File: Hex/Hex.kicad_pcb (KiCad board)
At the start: 2 copper layers, 114 x 88.2 mm, 39 parts, among them SW0x0 SW_Push, SW0x1 SW_Push, SW0x2 SW_Push, SW0x3 SW_Push, SW1x0 SW_Push, SW1x1 SW_Push, SW1x2 SW_Push, SW1x3 SW_Push, SW2x0 SW_Push, SW2x1 SW_Push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

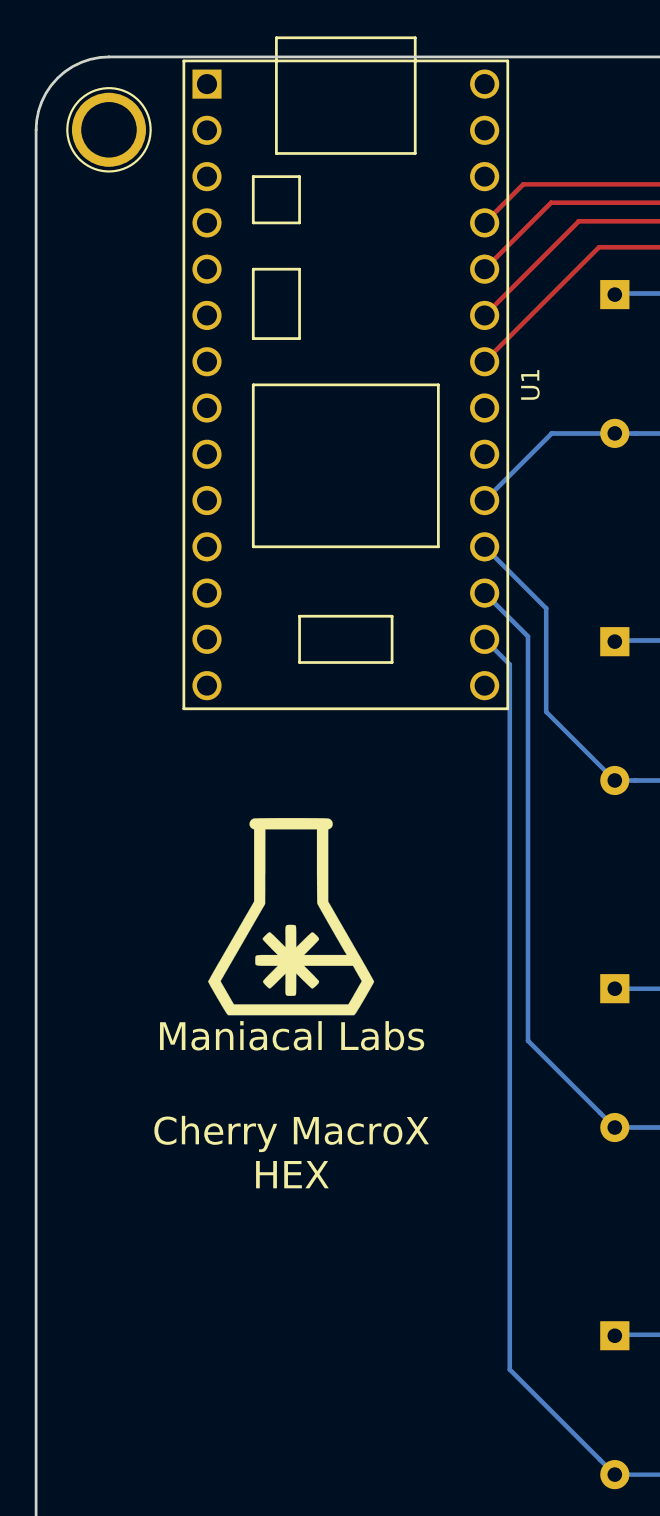
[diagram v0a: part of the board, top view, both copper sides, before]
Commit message: move logos
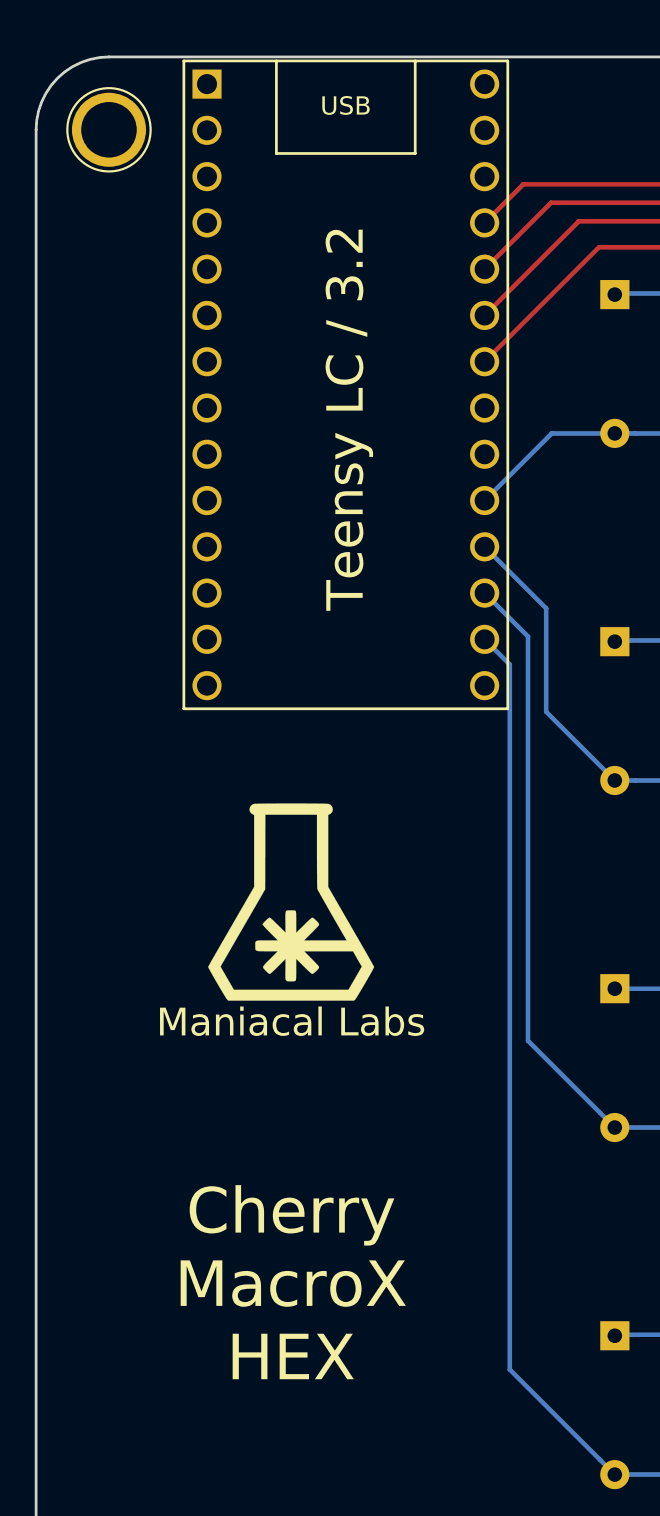
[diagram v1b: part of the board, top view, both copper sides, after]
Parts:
- moved L103 0.80 mm to (74.5, 84.0)
